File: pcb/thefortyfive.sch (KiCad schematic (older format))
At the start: 94 parts, among them J1 Conn_01x16_Female, J2 Conn_01x12_Female

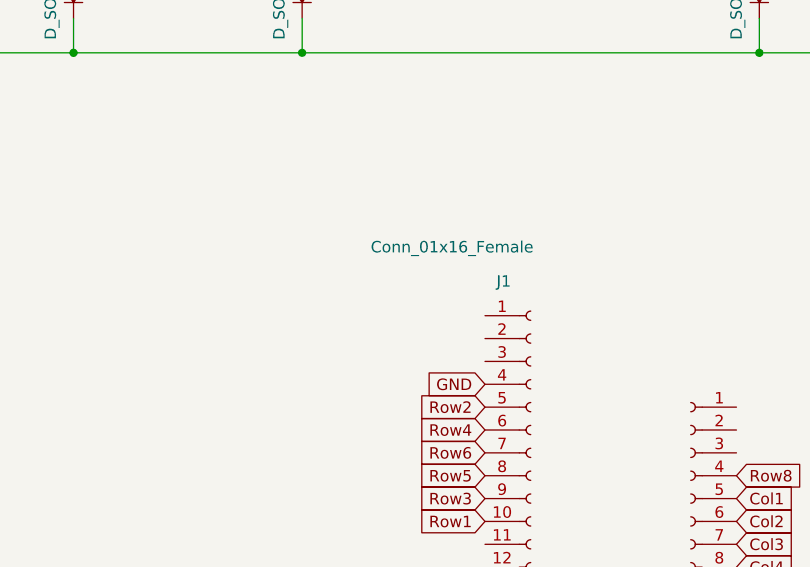
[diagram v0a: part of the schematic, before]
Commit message: added reset button
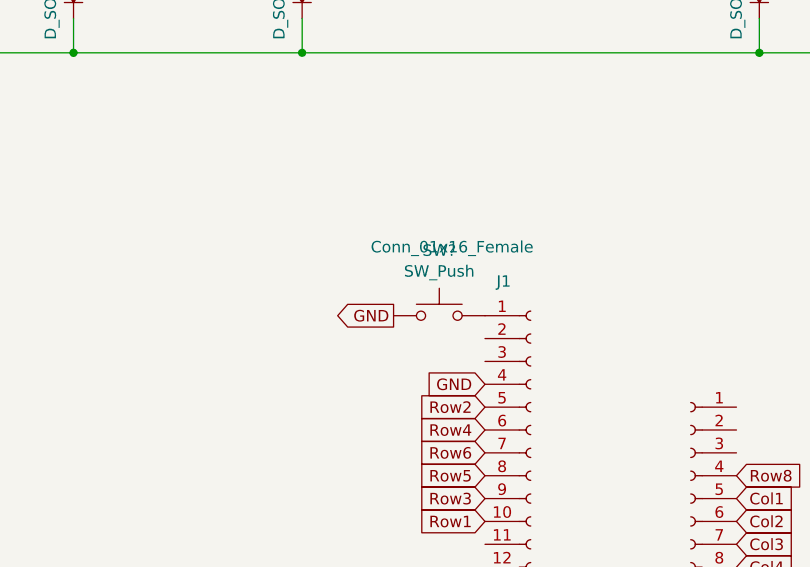
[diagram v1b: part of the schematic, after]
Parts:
- added SW?: SW_Push, symbol Switch:SW_Push
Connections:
- net GND: now also SW?.1
- net at J1.1 (Pin_1): now also SW?.2
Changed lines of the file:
@@
 Wire Wire Line
 	12800 7000 14200 7000
+$Comp
+L Switch:SW_Push SW?
+U 1 1 5E9F64B2
+P 5400 8150
+F 0 "SW?" H 5400 8435 50  0000 C CNN
+F 1 "SW_Push" H 5400 8344 50  0000 C CNN
+F 2 "" H 5400 8350 50  0001 C CNN
+F 3 "~" H 5400 8350 50  0001 C CNN
+	1    5400 8150
+	1    0    0    -1
+$EndComp
+Text GLabel 5200 8150 0    50   Output ~ 0
+GND
 $EndSCHEMATC
